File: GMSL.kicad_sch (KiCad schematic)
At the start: 11 parts, among them J2 Conn_FAKRA_59S2AQ-40MT5-Z_1

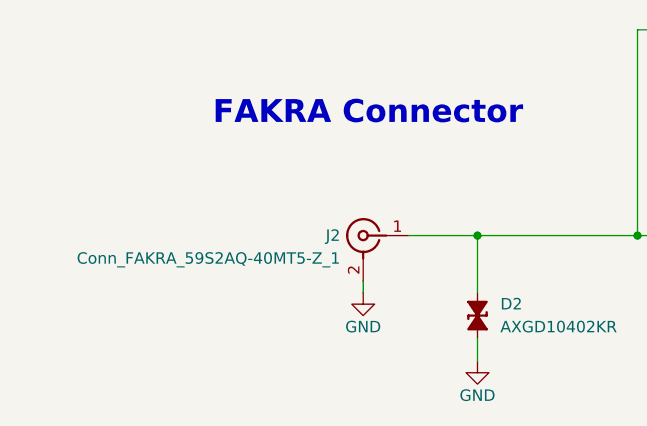
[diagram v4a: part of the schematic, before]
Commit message: [#66847] Show MPN insted value; Update description
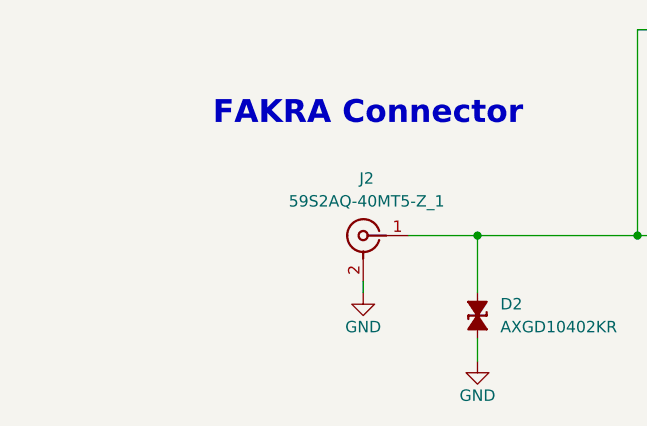
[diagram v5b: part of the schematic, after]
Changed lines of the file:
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@@
   )
   (symbol (lib_id "antmicroCoaxialConnectorsRF:Conn_FAKRA_59S2AQ-40MT5-Z_1") (at 125.73 111.76 0) (mirror y) (unit 1)
-    (in_bom yes) (on_board yes) (dnp no)
-    (property "Reference" "J2" (at 118.11 111.76 0)
-      (effects (font (size 1.27 1.27) (thickness 0.15)) (justify left))
+    (in_bom yes) (on_board yes) (dnp no) (fields_autoplaced)
+    (property "Reference" "J2" (at 121.0309 105.41 0)
+      (effects (font (size 1.27 1.27) (thickness 0.15)))
     )
     (property "Value" "Conn_FAKRA_59S2AQ-40MT5-Z_1" (at 118.11 114.3 0)
-      (effects (font (size 1.27 1.27) (thickness 0.15)) (justify left))
+      (effects (font (size 1.27 1.27) (thickness 0.15)) (justify left) hide)
     )
     (property "Footprint" "antmicro-footprints:Conn_FAKRA_59S2AQ-40MT5-Z_1" (at 105.41 121.92 0)
@@
       (effects (font (size 1.27 1.27) (thickness 0.15)) (justify left bottom) hide)
     )
-    (property "MPN" "59S2AQ-40MT5-Z_1" (at 105.41 127 0)
-      (effects (font (size 1.27 1.27) (thickness 0.15)) (justify left bottom) hide)
+    (property "MPN" "59S2AQ-40MT5-Z_1" (at 121.0309 107.95 0)
+      (effects (font (size 1.27 1.27) (thickness 0.15)))
     )
     (property "Manufacturer" "Rosenberger" (at 105.41 129.54 0)
